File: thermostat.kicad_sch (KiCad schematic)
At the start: 0 parts

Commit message: remove ref dac sheet, finish thermostat
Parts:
- added C? (x19): 100n, symbol Device:C
- added C? (x5): 10u, symbol Device:C
- added C? (x6): 1u, symbol Device:C
- added C?: 10u, symbol Device:C_Small
- added C? (x5): 10n, symbol Device:C
- added C?: C, symbol Device:C
- added C? (x2): 1u, symbol Device:C_Small
- added C? (x3): 100n, symbol Device:C_Small
- added C?: 220u, symbol Device:C_Polarized
- added D? (x2): BAV99, Package_TO_SOT_SMD:SOT-23, symbol Diode:BAV99
- added L? (x2): 6.8u, symbol Device:L
- added R?: 50m, symbol Device:R
- added R? (x4): 33, symbol Device:R
- added R? (x6): 10k, symbol Device:R
- added R? (x4): 51, symbol Device:R
- added R? (x2): 5k11 5ppm, symbol Device:R
- added R?: 1k6, symbol Device:R
- added U?: AD5680, Package_TO_SOT_SMD:SOT-23-8, symbol kirdy:AD5680
- added U?: AD7172-2, Package_SO:TSSOP-24_4.4x7.8mm_P0.65mm, symbol kirdy:AD7172-2
- added U?: ADP150AUJZ-3.3, Package_TO_SOT_SMD:TSOT-23-5, symbol kirdy:ADP150AUJZ-3.3
- added U?: MAX1968xUI, Package_SO:HTSSOP-28-1EP_4.4x9.7mm_P0.65mm_EP2.85x5.4mm, symbol Driver_TEC:MAX1968xUI
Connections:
- new net: C?.1, C?.1, U?.5 (REGCAPA)
- new net: R?.1, U?.3 (VFB), U?.4 (VOUT)
- new net: R?.1, U?.15 (OS1)
- new net: C?.1, R?.2, R?.2, U?.5 (VOUT)
- new net: C?.1, R?.1, R?.2 (x3)
- new net: C?.1, C?.1, R?.2, U?.1 (VIN), U?.3 (EN)
- new net: C?.1, C?.2, R?.1, U?.21 (AIN0)
- new net: C?.1, C?.2, D?.3 (K), R?.1, R?.2 (x2)
- new net: C?.1, C?.2, R?.1, U?.22 (AIN1)
- new net: C?.1, C?.1, U?.18 (REGCAPD)
- new net: C?.1, U?.4 (REFOUT)
- new net: L?.1, U?.10 (LX2), U?.6 (LX2), U?.8 (LX2)
- new net: C?.2, C?.2, U?.2 (GND)
- new net: C?.1, R?.2, U?.3 (CTLI)
- new net: L?.1, U?.19 (LX1), U?.21 (LX1), U?.23 (LX1)
- new net: C?.1, U?.25 (COMP)
- new net +3.3VA: D?.2 (A), D?.2 (A)
- new net +5V: C?.1, C?.1, C?.1, C?.1, U?.1 (VDD), U?.11 (PVDD2), U?.18 (PVDD1), U?.20 (PVDD1), U?.9 (PVDD2)
- new net +5VA: C?.1, C?.1, R?.1, U?.1 (VDD)
- new net ADC_A3V3: C?.1, C?.1, C?.1, R?.1, R?.2, U?.7 (AVDD1), U?.8 (AVDD2)
- new net ADC_CLKIO: U?.10 (XTAL2/CLKIO)
- new net ADC_D3V3: C?.1, C?.1, C?.1, R?.1, U?.16 (IOVDD)
- new net ADC_DIN: U?.12 (DIN)
- new net ADC_DOUT_~{RDY}: U?.11 (DOUT/~{RDY})
- new net ADC_REF: C?.1, C?.1, R?.1, R?.1, U?.2 (VREF), U?.3 (REF+)
- new net ADC_SCLK: U?.13 (SCLK)
- new net ADC_~{CS}: U?.14 (~{CS})
- new net ADC_~{SYNC}: U?.15 (~{SYNC}/~{ERR})
- new net DAC_DIN: U?.7 (DIN)
- new net DAC_SCLK: U?.6 (SCLK)
- new net DAC_~{SYNC}: U?.5 (~{SYNC})
- new net GND: C?.1, C?.1, C?.1, C?.1, C?.2, C?.2, C?.2, C?.2, C?.2, C?.2, C?.2, C?.2, C?.2, C?.2, C?.2, C?.2, C?.2, C?.2, C?.2, C?.2, C?.2, C?.2, C?.2, C?.2, C?.2, C?.2, C?.2, C?.2, C?.2, C?.2, C?.2, C?.2, C?.2, C?.2, C?.2, C?.2, C?.2, D?.1 (K), D?.1 (K), R?.2, U?.1 (AIN4), U?.12 (FREQ), U?.17 (DGND), U?.2 (GND), U?.2 (REF-), U?.22 (PGND), U?.23 (AIN2), U?.24 (AIN3), U?.24 (PGND), U?.29 (GND), U?.5 (PGND), U?.6 (AVSS), U?.7 (PGND), U?.8 (GND)
- new net MAXIN: C?.1, R?.2, U?.26 (MAXIN)
- new net MAXIP: C?.1, R?.2, U?.27 (MAXIP)
- new net MAXV: C?.1, R?.2, U?.28 (MAXV)
- new net NTC+: R?.2, R?.2
- new net NTC-: R?.1, R?.2
- new net PWM_MAXIN: R?.1
- new net PWM_MAXIP: R?.1
- new net PWM_MAXV: R?.1
- new net TEC+: C?.1, C?.1, C?.2, C?.2, L?.2, R?.2, U?.16 (CS)
- new net TEC-: C?.1, C?.1, C?.2, C?.2, L?.2, U?.14 (OS2)
- new net TEC_ISEN: U?.13 (ITEC)
- new net TEC_VREF: C?.1, U?.4 (REF)
- new net TEC_~{SHDN}: U?.17 (~{SHDN})
- no-connect marks 0 -> 3

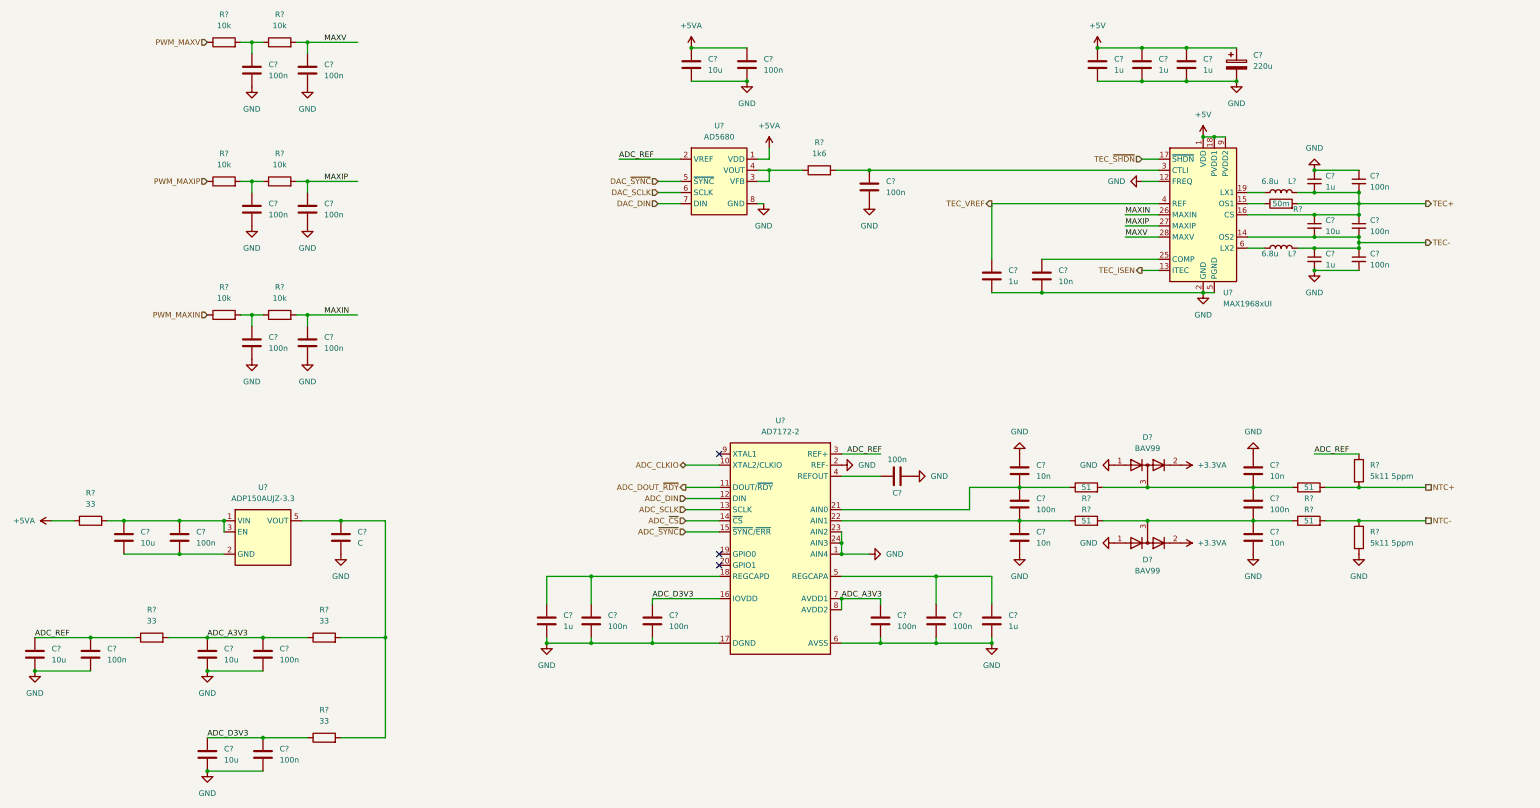
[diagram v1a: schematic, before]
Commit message: add TEC V sense, filter TEC I sense
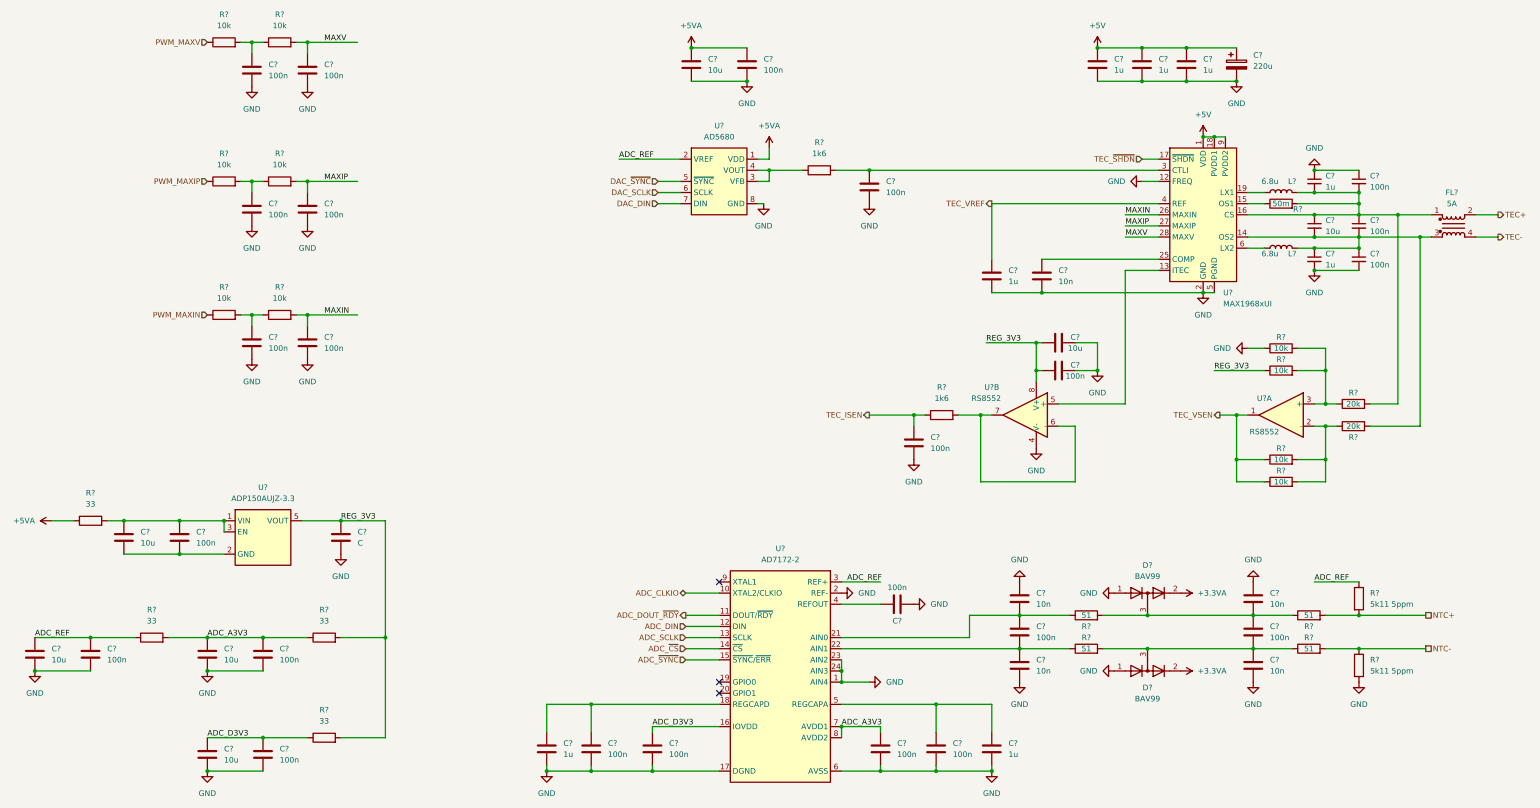
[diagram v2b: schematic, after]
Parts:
- added C? (x2): 100n, symbol Device:C
- added C?: 10u, symbol Device:C
- added FL?: 5A, symbol Device:Filter_EMI_CommonMode
- added R? (x4): 10k, symbol Device:R
- added R?: 1k6, symbol Device:R
- added R? (x2): 20k, symbol Device:R
- added U? (x3): RS8552, Package_SO:SOIC-8_3.9x4.9mm_P1.27mm, symbol kirdy:RS8552
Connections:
- net GND: now also C?.2, C?.2, C?.2, R?.1, U?.4 (V-)
- net TEC+: now also FL?.2; no longer C?.1, C?.1, C?.2, C?.2, L?.2, R?.2, U?.16 (CS)
- net TEC-: now also FL?.4; no longer C?.1, C?.1, C?.2, C?.2, L?.2, U?.14 (OS2)
- net TEC_ISEN: now also C?.1, R?.1; no longer U?.13 (ITEC)
- net REG_3V3: now reaches C?.1, R?.2, R?.2, U?.5 (VOUT)
- net REG_3V3: now also C?.1, C?.1, R?.1, U?.8 (V+)
- new net: C?.1, C?.1, C?.2, C?.2, FL?.1, L?.2, R?.2, R?.2, U?.16 (CS)
- new net: R?.1, R?.2, R?.2, U?.3 (+)
- new net: C?.1, C?.1, C?.2, C?.2, FL?.3, L?.2, R?.2, U?.14 (OS2)
- new net: R?.2, U?.6 (-), U?.7
- new net: U?.13 (ITEC), U?.5 (+)
- new net: R?.1, R?.2, R?.2, U?.2 (-)
- new net TEC_VSEN: R?.1, R?.1, U?.1
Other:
- moved on the sheet: C?, D?, R?, U?

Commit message: polish
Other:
- moved on the sheet: R?
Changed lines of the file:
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@@
     (stroke (width 0) (type default) (color 0 0 0 0))
   )
-  (wire (pts (xy 245.11 147.32) (xy 250.19 147.32))
+  (wire (pts (xy 246.38 147.32) (xy 250.19 147.32))
     (stroke (width 0) (type default) (color 0 0 0 0))
   )
@@
     (stroke (width 0) (type default) (color 0 0 0 0))
   )
-  (wire (pts (xy 234.95 147.32) (xy 237.49 147.32))
+  (wire (pts (xy 234.95 147.32) (xy 238.76 147.32))
     (stroke (width 0) (type default) (color 0 0 0 0))
   )
@@
     (pin "2")
   )
-  (symbol (lib_id "Device:R") (at 241.3 147.32 90) (unit 1)
-    (in_bom yes) (on_board yes) (fields_autoplaced)
-    (property "Reference" "R?" (id 0) (at 241.3 140.97 90))
-    (property "Value" "1k6" (id 1) (at 241.3 143.51 90))
-    (property "Footprint" "" (id 2) (at 241.3 149.098 90)
-      (effects (font (size 1.27 1.27)) hide)
-    )
-    (property "Datasheet" "~" (id 3) (at 241.3 147.32 0)
-      (effects (font (size 1.27 1.27)) hide)
-    )
+  (symbol (lib_id "Device:R") (at 242.57 147.32 90) (unit 1)
+    (in_bom yes) (on_board yes) (fields_autoplaced)
+    (property "Reference" "R?" (id 0) (at 242.57 140.97 90))
+    (property "Value" "1k6" (id 1) (at 242.57 143.51 90))
+    (property "Footprint" "" (id 2) (at 242.57 149.098 90)
+      (effects (font (size 1.27 1.27)) hide)
+    )
+    (property "Datasheet" "~" (id 3) (at 242.57 147.32 0)
+      (effects (font (size 1.27 1.27)) hide)
+    )

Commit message: before beer
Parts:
- removed C?: 100n, symbol Device:C
- removed C?: C, symbol Device:C
- removed C?: 10u, symbol Device:C
- removed R?: 33, symbol Device:R
- removed U?: ADP150AUJZ-3.3, Package_TO_SOT_SMD:TSOT-23-5, symbol kirdy:ADP150AUJZ-3.3
- added C?: 10u, symbol Device:C
- added C?: 100n, symbol Device:C
- added R?: 33, symbol Device:R
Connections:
- net REG_3V3 is gone; now on net +3.3VA: C?.1, C?.1, R?.1, R?.2, R?.2, U?.8 (V+)
- net ADC_A3V3: now also R?.2
- net ADC_REF: no longer U?.2 (VREF)
- net GND: now also C?.2, C?.2
- new net DAC_REF: C?.1, C?.1, R?.1, U?.2 (VREF)

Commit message: add USB
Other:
- company: (none) -> M-Labs
- title: (none) -> Kirdy
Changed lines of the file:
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@@
 (kicad_sch (version 20211123) (generator eeschema)
   (paper "A3")
+  (title_block
+    (title "Kirdy")
+    (date "2022-07-03")
+    (rev "r0.1")
+    (company "M-Labs")
+    (comment 1 "Alex Wong Tat Hang")
+  )
   (junction (at 300.99 119.38) (diameter 0) (color 0 0 0 0)
   )

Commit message: complete mcu
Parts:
- gave numbers to parts that had none: 79

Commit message: first draft complete
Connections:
- net ADC_CLKIO: no longer names the net of U18.10 (XTAL2/CLKIO)
- no-connect marks 3 -> 4
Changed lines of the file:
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@@
   )
   (no_connect (at 190.5 185.42))
+  (no_connect (at 190.5 187.96))
   (no_connect (at 190.5 208.28))
   (no_connect (at 190.5 210.82))
@@
     (stroke (width 0) (type default) (color 0 0 0 0))
   )
-  (wire (pts (xy 182.88 187.96) (xy 190.5 187.96))
-    (stroke (width 0) (type default) (color 0 0 0 0))
-  )
   (wire (pts (xy 151.13 227.33) (xy 151.13 228.6))
     (stroke (width 0) (type default) (color 0 0 0 0))
@@
   )
   (hierarchical_label "ADC_DOUT_~{RDY}" (shape output) (at 182.88 193.04 180)
-    (effects (font (size 1.27 1.27)) (justify right))
-  )
-  (hierarchical_label "ADC_CLKIO" (shape bidirectional) (at 182.88 187.96 180)
     (effects (font (size 1.27 1.27)) (justify right))
   )
@@
     (pin "1")
     (pin "2")
+  )
+  (symbol (lib_id "power:PWR_FLAG") (at 86.36 220.98 0) (unit 1)
+    (in_bom yes) (on_board yes) (fields_autoplaced)
+    (property "Reference" "#FLG0113" (id 0) (at 86.36 219.075 0)
+      (effects (font (size 1.27 1.27)) hide)
+    )
+    (property "Value" "PWR_FLAG" (id 1) (at 86.36 215.9 0)
+      (effects (font (size 1.27 1.27)) hide)
+    )
+    (property "Footprint" "" (id 2) (at 86.36 220.98 0)
+      (effects (font (size 1.27 1.27)) hide)
+    )
+    (property "Datasheet" "~" (id 3) (at 86.36 220.98 0)
+      (effects (font (size 1.27 1.27)) hide)
+    )
+    (pin "1")
   )
   (symbol (lib_id "Device:C") (at 161.29 223.52 0) (unit 1)
@@
     (pin "2")
   )
+  (symbol (lib_id "power:PWR_FLAG") (at 86.36 198.12 0) (unit 1)
+    (in_bom yes) (on_board yes) (fields_autoplaced)
+    (property "Reference" "#FLG0114" (id 0) (at 86.36 196.215 0)
+      (effects (font (size 1.27 1.27)) hide)
+    )
+    (property "Value" "PWR_FLAG" (id 1) (at 86.36 193.04 0)
+      (effects (font (size 1.27 1.27)) hide)
+    )
+    (property "Footprint" "" (id 2) (at 86.36 198.12 0)
+      (effects (font (size 1.27 1.27)) hide)
+    )
+    (property "Datasheet" "~" (id 3) (at 86.36 198.12 0)
+      (effects (font (size 1.27 1.27)) hide)
+    )
+    (pin "1")
+  )
   (symbol (lib_id "kirdy:RS8552") (at 260.35 147.32 0) (mirror y) (unit 2)
